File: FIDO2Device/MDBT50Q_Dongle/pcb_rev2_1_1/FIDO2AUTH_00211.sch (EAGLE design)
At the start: 35 parts, among them CN1 TE-1734028, CN2 IF_5PIN_H, CN3 IF_3PIN, SW1 SKRPACE010, SW2 SKTADAE010, U1 MDBT50Q-P1M, U2 XC6206P332MR-G, X1 NX3215SA-32.768K

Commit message: 回路図を修正
・ドキュメントタイトル修正、シート追加
・部品の小型化（リセット回路、差動信号回路、LED回路）
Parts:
- C5, C7, C8, C9: device Parts:CAP_0603 -> Parts:CAP_0402
- R1, R2, R3, R4, R5, R6: device Parts:RESISTOR_0603 -> Parts:RESISTOR_0402
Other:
- note added: "MDBT50Q Dongle （rev2.1.1）"
- note added: "MDBT50Q-P1M Dongle rev2.1.1"
- note added: "セキュリティーIC部"
- note removed: "MDBT50Q Dongle （rev2）"
- note removed: "MDBT50Q-P1M Dongle rev2"
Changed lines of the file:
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@@
 <setting verticaltext="up"/>
 </settings>
-<grid distance="0.1" unitdist="inch" unit="inch" style="lines" multiple="1" display="yes" altdistance="0.01" altunitdist="inch" altunit="inch"/>
+<grid distance="0.1" unitdist="inch" unit="inch" style="lines" multiple="1" display="no" altdistance="0.01" altunitdist="inch" altunit="inch"/>
 <layers>
 <layer number="1" name="Top" color="4" fill="1" visible="no" active="no"/>
@@
 <part name="FB1" library="Parts" deviceset="BLM15AG" device="121SN1D"/>
 <part name="FB2" library="Parts" deviceset="BLM15AG" device="121SN1D"/>
-<part name="C5" library="Parts" deviceset="CAP" device="_0603" value="0.01uF"/>
+<part name="C5" library="Parts" deviceset="CAP" device="_0402" value="0.01uF"/>
 <part name="C6" library="Parts" deviceset="CAP" device="_0603" value="10uF"/>
-<part name="C7" library="Parts" deviceset="CAP" device="_0603" value="0.1uF"/>
-<part name="C8" library="Parts" deviceset="CAP" device="_0603" value="0.1uF"/>
+<part name="C7" library="Parts" deviceset="CAP" device="_0402" value="0.1uF"/>
+<part name="C8" library="Parts" deviceset="CAP" device="_0402" value="0.1uF"/>
 <part name="GND8" library="Supply" deviceset="0V" device=""/>
 <part name="GND9" library="Supply" deviceset="0V" device=""/>
@@
 <part name="D1" library="Parts" deviceset="PRTR5V0U2X" device=""/>
 <part name="CN1" library="Connectors" deviceset="TE-1734028" device=""/>
-<part name="R1" library="Parts" deviceset="RESISTOR" device="_0603" value="10k"/>
-<part name="C9" library="Parts" deviceset="CAP" device="_0603" value="0.1uF"/>
+<part name="R1" library="Parts" deviceset="RESISTOR" device="_0402" value="10k"/>
+<part name="C9" library="Parts" deviceset="CAP" device="_0402" value="0.1uF"/>
 <part name="GND11" library="Supply" deviceset="0V" device=""/>
 <part name="SW1" library="Parts" deviceset="SKRPACE010" device=""/>
@@
 <part name="LED1" library="Parts" deviceset="APHD1608" device="LSURCK"/>
 <part name="LED2" library="Parts" deviceset="APHF1608" device="LSEEQBDZGKC"/>
-<part name="R2" library="Parts" deviceset="RESISTOR" device="_0603" value="1.5k"/>
-<part name="R3" library="Parts" deviceset="RESISTOR" device="_0603" value="1.2k"/>
-<part name="R4" library="Parts" deviceset="RESISTOR" device="_0603" value="2.2k"/>
-<part name="R5" library="Parts" deviceset="RESISTOR" device="_0603" value="390"/>
+<part name="R2" library="Parts" deviceset="RESISTOR" device="_0402" value="1.5k"/>
+<part name="R3" library="Parts" deviceset="RESISTOR" device="_0402" value="1.2k"/>
+<part name="R4" library="Parts" deviceset="RESISTOR" device="_0402" value="2.2k"/>
+<part name="R5" library="Parts" deviceset="RESISTOR" device="_0402" value="390"/>
 <part name="CN2" library="Connectors" deviceset="IF_5PIN" device="_H"/>
 <part name="GND14" library="Supply" deviceset="0V" device=""/>
@@
 <part name="GND19" library="Supply" deviceset="0V" device=""/>
 <part name="LED3" library="Parts" deviceset="APTD1608" device="LSYCK"/>
-<part name="R6" library="Parts" deviceset="RESISTOR" device="_0603" value="1.5k"/>
+<part name="R6" library="Parts" deviceset="RESISTOR" device="_0402" value="1.5k"/>
+<part name="FRAME4" library="Generic" deviceset="A4L-LOC" device=""/>
 </parts>
 <sheets>
@@
 <text x="152.4" y="152.4" size="2.54" layer="91">32.768kHzクリスタル</text>
 <text x="203.2" y="152.4" size="2.54" layer="91">バイパスコンデンサー</text>
-<text x="218.44" y="20.32" size="1.778" layer="91">MDBT50Q-P1M Dongle rev2</text>
+<text x="217.424" y="20.32" size="1.778" layer="91">MDBT50Q-P1M Dongle rev2.1.1</text>
 <text x="166.37" y="8.89" size="3.81" layer="91">MDBT50Q Dongle
-      （rev2）</text>
+    （rev2.1.1）</text>
 <text x="20.32" y="162.56" size="3.81" layer="91">モジュール部</text>
 <text x="167.64" y="91.44" size="2.54" layer="91">リセット回路</text>
@@
 <text x="152.4" y="81.28" size="2.54" layer="91">nRF52840アプリケーションを
 書込する際に使用します。</text>
-<text x="218.44" y="20.32" size="1.778" layer="91">MDBT50Q-P1M Dongle rev2</text>
+<text x="217.424" y="20.32" size="1.778" layer="91">MDBT50Q-P1M Dongle rev2.1.1</text>
 <text x="166.37" y="8.89" size="3.81" layer="91">MDBT50Q Dongle
-      （rev2）</text>
+    （rev2.1.1）</text>
 <text x="124.46" y="66.04" size="2.54" layer="91">LED（黄色）</text>
 <text x="40.64" y="66.04" size="2.54" layer="91">LED（赤色）</text>
@@
 <text x="78.74" y="60.96" size="2.54" layer="91">ボタン乾電池ケースは
 基板の背面に実装</text>
-<text x="218.44" y="20.32" size="1.778" layer="91">MDBT50Q-P1M Dongle rev2</text>
+<text x="217.424" y="20.32" size="1.778" layer="91">MDBT50Q-P1M Dongle rev2.1.1</text>
 <text x="166.37" y="8.89" size="3.81" layer="91">MDBT50Q Dongle
-      （rev2）</text>
+    （rev2.1.1）</text>
 </plain>
 <instances>
@@
 </nets>
 </sheet>
+<sheet>
+<plain>
+<text x="217.424" y="20.32" size="1.778" layer="91">MDBT50Q-P1M Dongle rev2.1.1</text>
+<text x="166.37" y="8.89" size="3.81" layer="91">MDBT50Q Dongle
+    （rev2.1.1）</text>
+<text x="45.72" y="142.24" size="3.81" layer="91">セキュリティーIC部</text>
+</plain>
+<instances>
+<instance part="FRAME4" gate="G$1" x="0" y="0"/>
+</instances>
+<busses>
+</busses>
+<nets>
+</nets>
+</sheet>

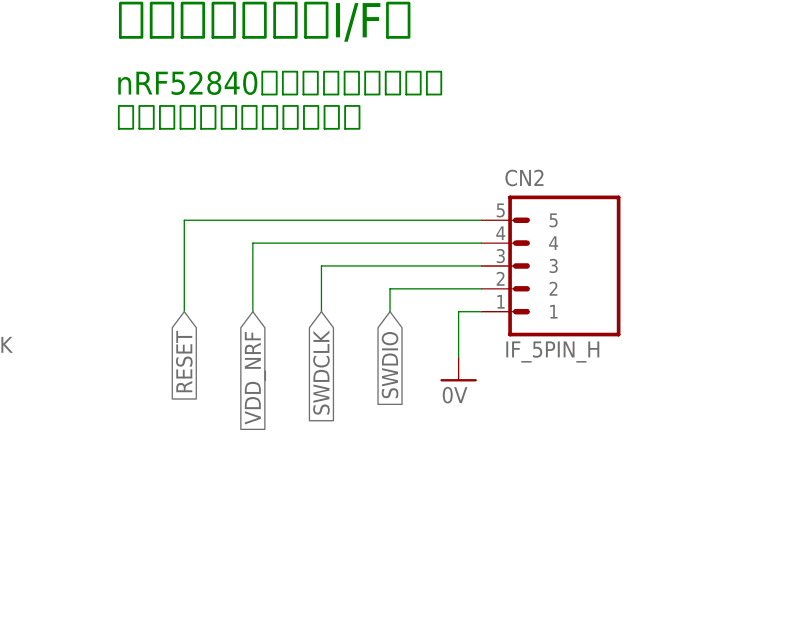
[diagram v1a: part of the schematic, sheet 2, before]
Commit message: 回路図を修正
・TWI_SDA、TWI_SCLを、実機動作確認結果を元に割り当て
・汎用I/Oを新規に２点割り当て
・プログラム用ピンの配置を修正
（RESETは不要なので廃止、VDDの位置をnRF52840 DK上の順列に合わせる）
・ERC、DRCともにOKを確認
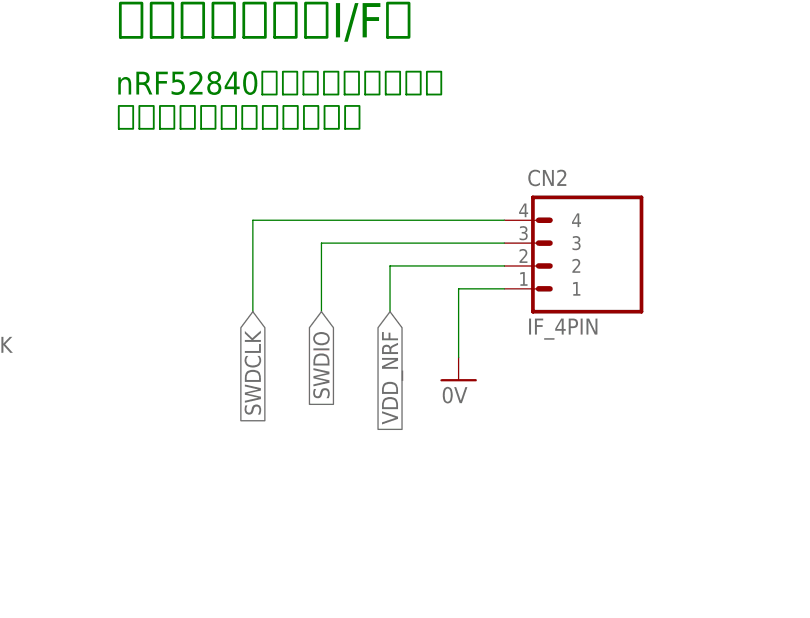
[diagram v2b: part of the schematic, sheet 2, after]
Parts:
- added CN4: IF_3PIN_SOL, Connectors:IF_3PIN_SOL
- CN2: value IF_5PIN_H -> IF_4PIN; device Connectors:IF_5PIN_H -> Connectors:IF_4PIN
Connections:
- net AIN0 renamed TWI_SCL
- net UART_TX renamed TWI_SDA
- new net P0.03: CN4.3, U1.P0.03/AIN1
- new net P1.14: CN4.2, U1.P1.14
- net 0V: now also CN4.1
- net RESET: no longer CN2.5
- net SWDCLK: now also CN2.4; no longer CN2.3
- net SWDIO: now also CN2.3; no longer CN2.2
- net VDD_NRF: now also CN2.2; no longer CN2.4
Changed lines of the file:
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@@
 <part name="R4" library="Parts" deviceset="RESISTOR" device="_0402" value="2.2k"/>
 <part name="R5" library="Parts" deviceset="RESISTOR" device="_0402" value="390"/>
-<part name="CN2" library="Connectors" deviceset="IF_5PIN" device="_H"/>
 <part name="GND14" library="Supply" deviceset="0V" device=""/>
 <part name="FRAME3" library="Generic" deviceset="A4L-LOC" device=""/>
@@
 <part name="R6" library="Parts" deviceset="RESISTOR" device="_0402" value="1.5k"/>
 <part name="FRAME4" library="Generic" deviceset="A4L-LOC" device=""/>
+<part name="CN4" library="Connectors" deviceset="IF_3PIN" device="_SOL" value="IF_3PIN_SOL"/>
+<part name="GND20" library="Supply" deviceset="0V" device=""/>
+<part name="CN2" library="Connectors" deviceset="IF_4PIN" device=""/>
 </parts>
 <sheets>
@@
 </segment>
 </net>
-<net name="AIN0" class="0">
+<net name="TWI_SCL" class="0">
 <segment>
 <pinref part="U1" gate="G$1" pin="P0.02/AIN0"/>
@@
 </segment>
 </net>
-<net name="UART_TX" class="0">
+<net name="TWI_SDA" class="0">
 <segment>
 <pinref part="U1" gate="G$1" pin="P0.06"/>
@@
 <wire x1="60.96" y1="27.94" x2="45.72" y2="27.94" width="0.1524" layer="91"/>
 <label x="45.72" y="27.94" size="1.778" layer="95" rot="R180" xref="yes"/>
+</segment>
+</net>
+<net name="P0.03" class="0">
+<segment>
+<pinref part="U1" gate="G$1" pin="P0.03/AIN1"/>
+<wire x1="43.18" y1="91.44" x2="35.56" y2="91.44" width="0.1524" layer="91"/>
+<label x="35.56" y="91.44" size="1.778" layer="95" rot="R180" xref="yes"/>
+</segment>
+</net>
+<net name="P1.14" class="0">
+<segment>
+<pinref part="U1" gate="G$1" pin="P1.14"/>
+<wire x1="43.18" y1="96.52" x2="35.56" y2="96.52" width="0.1524" layer="91"/>
+<label x="35.56" y="96.52" size="1.778" layer="95" rot="R180" xref="yes"/>
 </segment>
 </net>
@@
 <instance part="R4" gate="G$1" x="73.66" y="40.64" rot="R90"/>
 <instance part="R5" gate="G$1" x="83.82" y="40.64" rot="R90"/>
-<instance part="CN2" gate="G$1" x="193.04" y="71.12"/>
 <instance part="GND14" gate="1" x="190.5" y="53.34"/>
 <instance part="LED3" gate="G$1" x="119.38" y="60.96" smashed="yes">
@@
 </instance>
 <instance part="R6" gate="G$1" x="119.38" y="40.64" rot="R90"/>
+<instance part="CN2" gate="G$1" x="195.58" y="71.12"/>
 </instances>
 <busses>
@@
 <segment>
 <pinref part="GND14" gate="1" pin="0V"/>
-<wire x1="190.5" y1="55.88" x2="190.5" y2="60.96" width="0.1524" layer="91"/>
+<wire x1="190.5" y1="55.88" x2="190.5" y2="63.5" width="0.1524" layer="91"/>
 <pinref part="CN2" gate="G$1" pin="1"/>
-<wire x1="190.5" y1="60.96" x2="193.04" y2="60.96" width="0.1524" layer="91"/>
+<wire x1="190.5" y1="63.5" x2="195.58" y2="63.5" width="0.1524" layer="91"/>
 </segment>
 </net>
@@
 </segment>
 <segment>
-<pinref part="CN2" gate="G$1" pin="4"/>
-<wire x1="193.04" y1="68.58" x2="167.64" y2="68.58" width="0.1524" layer="91"/>
-<wire x1="167.64" y1="68.58" x2="167.64" y2="60.96" width="0.1524" layer="91"/>
-<label x="167.64" y="60.96" size="1.778" layer="95" rot="R270" xref="yes"/>
+<wire x1="182.88" y1="66.04" x2="182.88" y2="60.96" width="0.1524" layer="91"/>
+<label x="182.88" y="60.96" size="1.778" layer="95" rot="R270" xref="yes"/>
+<pinref part="CN2" gate="G$1" pin="2"/>
+<wire x1="195.58" y1="66.04" x2="182.88" y2="66.04" width="0.1524" layer="91"/>
 </segment>
 <segment>
@@
 <net name="SWDIO" class="0">
 <segment>
-<pinref part="CN2" gate="G$1" pin="2"/>
-<wire x1="193.04" y1="63.5" x2="182.88" y2="63.5" width="0.1524" layer="91"/>
-<wire x1="182.88" y1="63.5" x2="182.88" y2="60.96" width="0.1524" layer="91"/>
-<label x="182.88" y="60.96" size="1.778" layer="95" rot="R270" xref="yes"/>
+<wire x1="175.26" y1="68.58" x2="175.26" y2="60.96" width="0.1524" layer="91"/>
+<label x="175.26" y="60.96" size="1.778" layer="95" rot="R270" xref="yes"/>
+<pinref part="CN2" gate="G$1" pin="3"/>
+<wire x1="195.58" y1="68.58" x2="175.26" y2="68.58" width="0.1524" layer="91"/>
 </segment>
 </net>
 <net name="SWDCLK" class="0">
 <segment>
-<pinref part="CN2" gate="G$1" pin="3"/>
-<wire x1="193.04" y1="66.04" x2="175.26" y2="66.04" width="0.1524" layer="91"/>
-<wire x1="175.26" y1="66.04" x2="175.26" y2="60.96" width="0.1524" layer="91"/>
-<label x="175.26" y="60.96" size="1.778" layer="95" rot="R270" xref="yes"/>
-</segment>
-</net>
-<net name="RESET" class="0">
-<segment>
-<pinref part="CN2" gate="G$1" pin="5"/>
-<wire x1="193.04" y1="71.12" x2="160.02" y2="71.12" width="0.1524" layer="91"/>
-<wire x1="160.02" y1="71.12" x2="160.02" y2="60.96" width="0.1524" layer="91"/>
-<label x="160.02" y="60.96" size="1.778" layer="95" rot="R270" xref="yes"/>
+<wire x1="167.64" y1="71.12" x2="167.64" y2="60.96" width="0.1524" layer="91"/>
+<label x="167.64" y="60.96" size="1.778" layer="95" rot="R270" xref="yes"/>
+<pinref part="CN2" gate="G$1" pin="4"/>
+<wire x1="195.58" y1="71.12" x2="167.64" y2="71.12" width="0.1524" layer="91"/>
 </segment>
 </net>
@@
 <instance part="CN3" gate="G$1" x="203.2" y="68.58"/>
 <instance part="GND19" gate="1" x="195.58" y="55.88"/>
+<instance part="CN4" gate="G$1" x="203.2" y="116.84"/>
+<instance part="GND20" gate="1" x="195.58" y="104.14"/>
 </instances>
 <busses>
@@
 <wire x1="203.2" y1="63.5" x2="195.58" y2="63.5" width="0.1524" layer="91"/>
 <wire x1="195.58" y1="63.5" x2="195.58" y2="58.42" width="0.1524" layer="91"/>
+</segment>
+<segment>
+<pinref part="CN4" gate="G$1" pin="1"/>
+<wire x1="203.2" y1="111.76" x2="195.58" y2="111.76" width="0.1524" layer="91"/>
+<wire x1="195.58" y1="111.76" x2="195.58" y2="106.68" width="0.1524" layer="91"/>
+<pinref part="GND20" gate="1" pin="0V"/>
 </segment>
 </net>
@@
 </segment>
 </net>
-<net name="UART_TX" class="0">
+<net name="TWI_SDA" class="0">
 <segment>
 <pinref part="CN3" gate="G$1" pin="2"/>
@@
 </segment>
 </net>
-<net name="AIN0" class="0">
+<net name="TWI_SCL" class="0">
 <segment>
 <pinref part="CN3" gate="G$1" pin="3"/>
@@
 </segment>
 </net>
+<net name="P0.03" class="0">
+<segment>
+<pinref part="CN4" gate="G$1" pin="3"/>
+<wire x1="203.2" y1="116.84" x2="195.58" y2="116.84" width="0.1524" layer="91"/>
+<wire x1="195.58" y1="116.84" x2="195.58" y2="124.46" width="0.1524" layer="91"/>
+<label x="195.58" y="124.46" size="1.778" layer="95" rot="R90" xref="yes"/>
+</segment>
+</net>
+<net name="P1.14" class="0">
+<segment>
+<pinref part="CN4" gate="G$1" pin="2"/>
+<wire x1="203.2" y1="114.3" x2="190.5" y2="114.3" width="0.1524" layer="91"/>
+<label x="190.5" y="114.3" size="1.778" layer="95" rot="R180" xref="yes"/>
+</segment>
+</net>

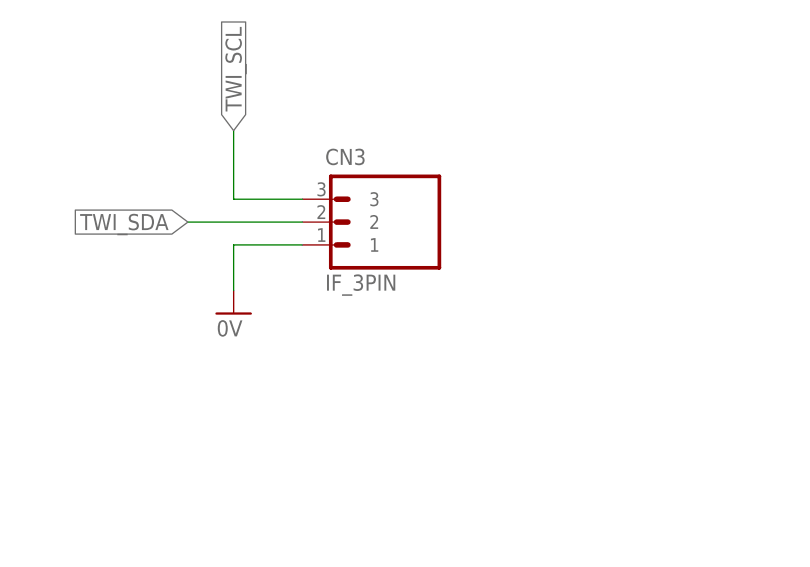
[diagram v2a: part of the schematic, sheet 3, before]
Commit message: 回路図を修正
・汎用ピンのブレークアウトを、スルーホールを裏面パッドに変更
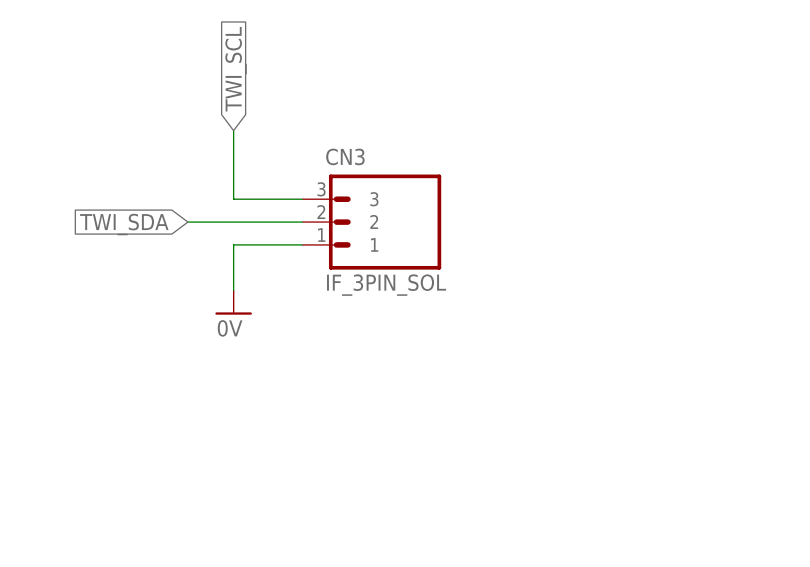
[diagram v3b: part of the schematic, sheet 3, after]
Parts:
- CN3: value IF_3PIN -> IF_3PIN_SOL; device Connectors:IF_3PIN -> Connectors:IF_3PIN_SOL
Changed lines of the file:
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@@
 <part name="BAT1" library="Connectors" deviceset="BAT-HLD-012-SMT" device=""/>
 <part name="GND18" library="Supply" deviceset="0V" device=""/>
-<part name="CN3" library="Connectors" deviceset="IF_3PIN" device=""/>
+<part name="CN3" library="Connectors" deviceset="IF_3PIN" device="_SOL" value="IF_3PIN_SOL"/>
 <part name="GND19" library="Supply" deviceset="0V" device=""/>
 <part name="LED3" library="Parts" deviceset="APTD1608" device="LSYCK"/>
